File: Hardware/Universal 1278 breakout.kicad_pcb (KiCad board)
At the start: 2 copper layers, 26.7 x 30.6 mm, 7 parts, among them J1 Conn_Coaxial, J2 Conn_01x10, J3 Conn_01x10, U1 XL1278-SMT, U2 DRF1278F

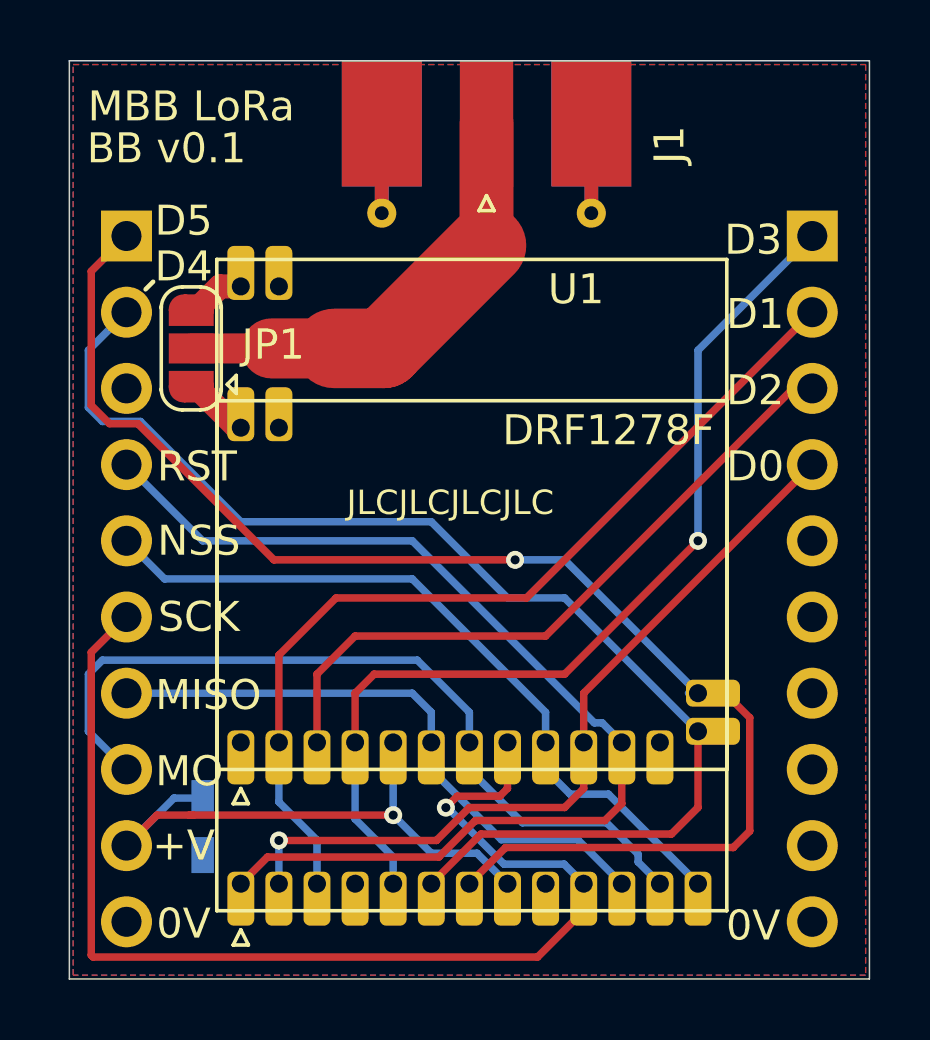
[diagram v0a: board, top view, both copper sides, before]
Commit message: Fix all DRC violations - missing connections
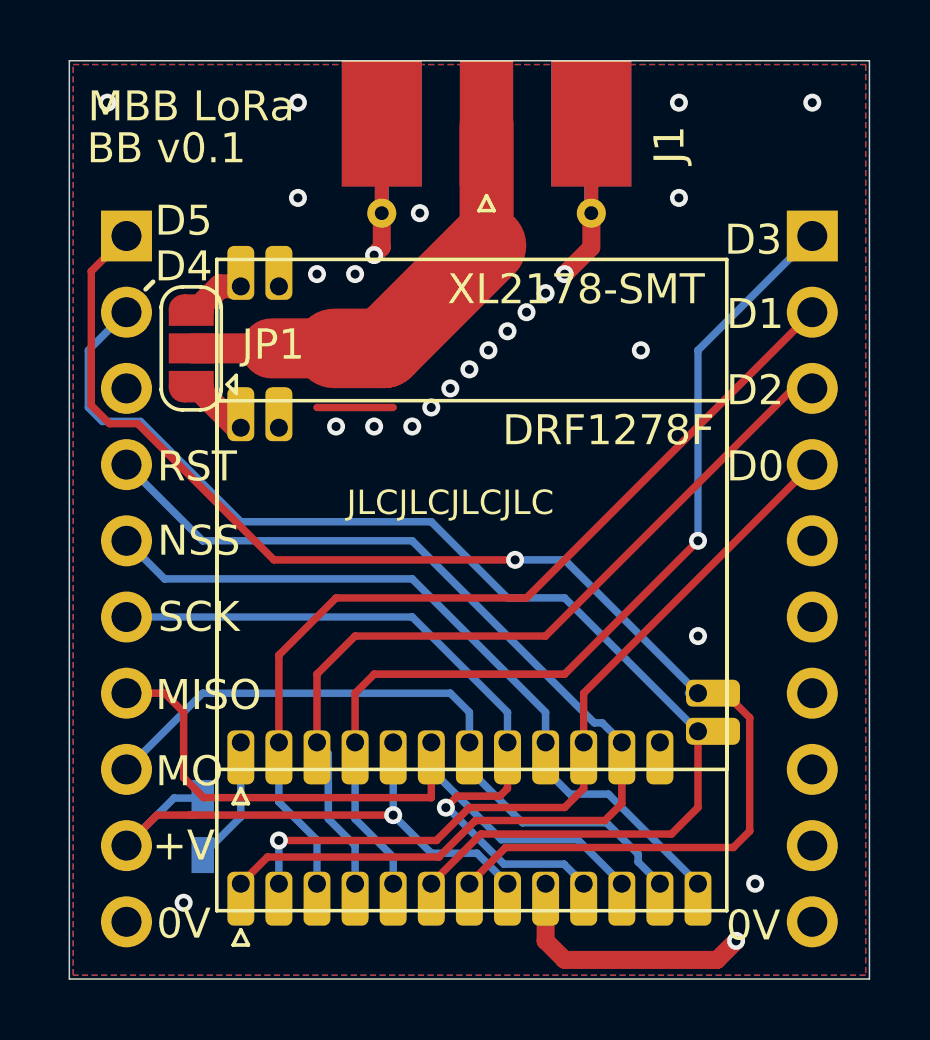
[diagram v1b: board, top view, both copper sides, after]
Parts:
- renumbered U1 to XL2178-SMT
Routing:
- net GND: track 0.00 -> 17.0 mm, vias 0 -> 26
- net SCK: track 39.3 -> 25.5 mm
- net DIO2: track 22.7 -> 28.0 mm
- net MOSI: track 27.6 -> 23.0 mm
- net MISO: track 20.3 -> 23.6 mm
- net (no net): track 0.00 -> 2.54 mm
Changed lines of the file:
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@@
     (thickness 1.6002)
     (drawings 28)
-    (tracks 140)
+    (tracks 180)
     (zones 0)
     (modules 7)
@@
   )
   (setup
-    (last_trace_width 0.127)
+    (last_trace_width 0.25)
     (user_trace_width 0.15)
     (user_trace_width 0.2)
@@
   (module "My footprints:XL1278-SMT" (layer Front)
     (at 143.51 99.06 90)
-    (fp_text reference U1 (at 12.192 14.986) (layer F.SilkS)
+    (fp_text reference XL2178-SMT (at 12.192 14.986) (layer F.SilkS)
       (effects (font (size 1 1) (thickness 0.15)))
     )
@@
     (arrow2b (pts (xy 143.51 116.84) (xy 144.636504 116.253579)))
   )
+  (segment (start 149.86 90.805) (end 152.4 90.805) (width 0.25) (layer Front) (net 0))
   (segment (start 145.669 88.8365) (end 148.336 88.8365) (width 1) (layer Front) (net 1))
   (segment (start 155.5115 81.3435) (end 155.5115 85.4075) (width 1.8) (layer Front) (net 1))
@@
   (segment (start 152.0825 88.8365) (end 155.5115 85.4075) (width 2.65) (layer Front) (net 1))
   (segment (start 150.4315 88.8365) (end 152.0825 88.8365) (width 2.65) (layer Front) (net 1))
+  (via (at 162.56 98.425) (size 0.6) (drill 0.3) (layers Front Back) (net 2))
+  (via (at 163.83 108.585) (size 0.6) (drill 0.3) (layers Front Back) (net 2))
+  (via (at 145.415 107.315) (size 0.6) (drill 0.3) (layers Front Back) (net 2))
+  (via (at 158.115 86.36) (size 0.6) (drill 0.3) (layers Front Back) (net 2))
+  (via (at 156.845 87.63) (size 0.6) (drill 0.3) (layers Front Back) (net 2))
+  (via (at 155.575 88.9) (size 0.6) (drill 0.3) (layers Front Back) (net 2))
+  (via (at 156.21 88.265) (size 0.6) (drill 0.3) (layers Front Back) (net 2))
+  (via (at 157.48 86.995) (size 0.6) (drill 0.3) (layers Front Back) (net 2))
+  (via (at 154.94 89.535) (size 0.6) (drill 0.3) (layers Front Back) (net 2))
+  (via (at 154.305 90.17) (size 0.6) (drill 0.3) (layers Front Back) (net 2))
+  (via (at 153.67 90.805) (size 0.6) (drill 0.3) (layers Front Back) (net 2))
+  (via (at 150.495 91.44) (size 0.6) (drill 0.3) (layers Front Back) (net 2))
+  (via (at 151.765 91.44) (size 0.6) (drill 0.3) (layers Front Back) (net 2))
+  (via (at 153.035 91.44) (size 0.6) (drill 0.3) (layers Front Back) (net 2))
+  (via (at 151.765 85.725) (size 0.6) (drill 0.3) (layers Front Back) (net 2))
+  (via (at 151.13 86.36) (size 0.6) (drill 0.3) (layers Front Back) (net 2))
+  (via (at 149.86 86.36) (size 0.6) (drill 0.3) (layers Front Back) (net 2))
+  (via (at 166.37 80.645) (size 0.6) (drill 0.3) (layers Front Back) (net 2))
+  (via (at 142.875 80.645) (size 0.6) (drill 0.3) (layers Front Back) (net 2))
+  (via (at 161.925 80.645) (size 0.6) (drill 0.3) (layers Front Back) (net 2))
+  (via (at 149.225 80.645) (size 0.6) (drill 0.3) (layers Front Back) (net 2))
+  (via (at 149.225 83.82) (size 0.6) (drill 0.3) (layers Front Back) (net 2))
+  (via (at 161.925 83.82) (size 0.6) (drill 0.3) (layers Front Back) (net 2))
+  (via (at 160.655 88.9) (size 0.6) (drill 0.3) (layers Front Back) (net 2))
+  (via (at 164.465 106.68) (size 0.6) (drill 0.3) (layers Front Back) (net 2))
+  (segment (start 159.004 85.471) (end 158.115 86.36) (width 0.6) (layer Front) (net 2))
+  (segment (start 159.004 84.3285) (end 159.004 85.471) (width 0.6) (layer Front) (net 2))
+  (segment (start 152.019 85.471) (end 151.765 85.725) (width 0.6) (layer Front) (net 2))
+  (segment (start 152.019 84.3285) (end 152.019 85.471) (width 0.6) (layer Front) (net 2))
+  (segment (start 157.48 106.68) (end 157.48 108.585) (width 0.6) (layer Front) (net 2))
+  (segment (start 157.48 108.585) (end 158.115 109.22) (width 0.6) (layer Front) (net 2))
+  (segment (start 163.195 109.22) (end 163.83 108.585) (width 0.6) (layer Front) (net 2))
+  (segment (start 158.115 109.22) (end 163.195 109.22) (width 0.6) (layer Front) (net 2))
+  (segment (start 147.32 104.455) (end 147.32 101.97) (width 0.25) (layer Back) (net 2))
+  (segment (start 146.05 105.725) (end 147.32 104.455) (width 0.25) (layer Back) (net 2))
+  (via (at 153.289 84.328) (size 0.6) (drill 0.3) (layers Front Back) (net 2))
   (segment (start 156.21 106.68) (end 155.194 105.664) (width 0.25) (layer Back) (net 3))
   (segment (start 155.194 105.664) (end 153.67 105.664) (width 0.25) (layer Back) (net 3))
@@
   (segment (start 160.56499 105.70099) (end 159.512 104.648) (width 0.25) (layer Back) (net 4))
   (segment (start 154.94 101.701828) (end 154.94 101.97) (width 0.25) (layer Back) (net 4))
-  (segment (start 142.707001 99.227999) (end 142.24 99.695) (width 0.25) (layer Back) (net 4))
-  (segment (start 153.202999 99.227999) (end 142.707001 99.227999) (width 0.25) (layer Back) (net 4))
-  (segment (start 154.94 100.965) (end 153.202999 99.227999) (width 0.25) (layer Back) (net 4))
   (segment (start 154.94 101.97) (end 154.94 100.965) (width 0.25) (layer Back) (net 4))
-  (segment (start 142.24 101.6) (end 143.51 102.87) (width 0.25) (layer Back) (net 4))
-  (segment (start 142.24 99.695) (end 142.24 101.6) (width 0.25) (layer Back) (net 4))
+  (segment (start 154.94 100.965) (end 154.305 100.33) (width 0.25) (layer Back) (net 4))
+  (segment (start 146.05 100.33) (end 143.51 102.87) (width 0.25) (layer Back) (net 4))
+  (segment (start 154.305 100.33) (end 146.05 100.33) (width 0.25) (layer Back) (net 4))
   (segment (start 153.67 102.877834) (end 153.67 101.97) (width 0.25) (layer Back) (net 5))
   (segment (start 156.006157 105.213991) (end 153.67 102.877834) (width 0.25) (layer Back) (net 5))
   (segment (start 158.553991 105.213991) (end 156.006157 105.213991) (width 0.25) (layer Back) (net 5))
   (segment (start 160.02 106.68) (end 158.553991 105.213991) (width 0.25) (layer Back) (net 5))
-  (segment (start 153.67 100.965) (end 153.67 101.97) (width 0.25) (layer Back) (net 5))
-  (segment (start 153.035 100.33) (end 153.67 100.965) (width 0.25) (layer Back) (net 5))
-  (segment (start 143.51 100.33) (end 153.035 100.33) (width 0.25) (layer Back) (net 5))
-  (segment (start 157.212833 109.125001) (end 158.75 107.587834) (width 0.25) (layer Front) (net 6))
-  (segment (start 142.334999 109.060999) (end 142.399001 109.125001) (width 0.25) (layer Front) (net 6))
+  (segment (start 153.67 101.97) (end 153.67 103.812392) (width 0.25) (layer Front) (net 5))
+  (segment (start 146.083354 103.812392) (end 145.415 103.144038) (width 0.25) (layer Front) (net 5))
+  (segment (start 153.67 103.812392) (end 146.083354 103.812392) (width 0.25) (layer Front) (net 5))
+  (segment (start 145.415 103.144038) (end 145.415 100.965) (width 0.25) (layer Front) (net 5))
+  (segment (start 145.415 100.965) (end 144.78 100.33) (width 0.25) (layer Front) (net 5))
+  (segment (start 144.78 100.33) (end 143.51 100.33) (width 0.25) (layer Front) (net 5))
   (segment (start 158.75 107.587834) (end 158.75 106.68) (width 0.25) (layer Front) (net 6))
-  (segment (start 142.334999 98.965001) (end 142.334999 109.060999) (width 0.25) (layer Front) (net 6))
-  (segment (start 142.399001 109.125001) (end 157.212833 109.125001) (width 0.25) (layer Front) (net 6))
-  (segment (start 143.51 97.79) (end 142.334999 98.965001) (width 0.25) (layer Front) (net 6))
   (segment (start 156.091162 106.02799) (end 154.203172 104.14) (width 0.25) (layer Back) (net 6))
   (segment (start 158.09799 106.02799) (end 156.091162 106.02799) (width 0.25) (layer Back) (net 6))
@@
   (segment (start 154.536364 103.76299) (end 154.155437 104.143917) (width 0.25) (layer Front) (net 6))
   (segment (start 155.95201 103.76299) (end 154.536364 103.76299) (width 0.25) (layer Front) (net 6))
+  (segment (start 156.21 101.97) (end 156.21 100.965) (width 0.25) (layer Back) (net 6))
+  (segment (start 153.035 97.79) (end 143.51 97.79) (width 0.25) (layer Back) (net 6))
+  (segment (start 156.21 100.965) (end 153.035 97.79) (width 0.25) (layer Back) (net 6))
   (segment (start 157.48 102.877834) (end 157.48 101.97) (width 0.25) (layer Back) (net 7))
   (segment (start 158.297176 103.69501) (end 157.48 102.877834) (width 0.25) (layer Back) (net 7))
@@
   (segment (start 165.735 90.17) (end 166.37 90.17) (width 0.25) (layer Front) (net 14))
   (segment (start 157.48 98.425) (end 165.735 90.17) (width 0.25) (layer Front) (net 14))
+  (segment (start 150.237009 102.347009) (end 150.237009 104.517009) (width 0.25) (layer Back) (net 14))
+  (segment (start 149.86 101.97) (end 150.237009 102.347009) (width 0.25) (layer Back) (net 14))
+  (segment (start 151.13 105.41) (end 151.13 106.68) (width 0.25) (layer Back) (net 14))
+  (segment (start 150.237009 104.517009) (end 151.13 105.41) (width 0.25) (layer Back) (net 14))
   (segment (start 158.75 101.97) (end 158.75 102.997) (width 0.25) (layer Front) (net 15))
   (segment (start 148.59 106.68) (end 148.59 107.696) (width 0.25) (layer Back) (net 15))
